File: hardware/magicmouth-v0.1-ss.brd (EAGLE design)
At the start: 100 x 80 mm, 28 parts, among them IC1 LM386N, IC2 ATMEGA168-20P, J1 1X2-3.5MM, Q1 16Mhz, U1 ARDUINOR3-NOIOREF-NOTEXT, X1 STEREOJACK

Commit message: added 5V jumper to v0.1 single sided board
added 5V jumper to v0.1 single sided board

added 5V jumper to v0.1 single sided board

added 5V jumper to v0.1 single sided board

added 5V jumper to v0.1 single sided board
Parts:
- moved C2 1.27 mm to (29.0, 55.9)
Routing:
- net N$5: track 21.8 -> 11.1 mm
- net +5V: track 78.5 -> 74.6 mm, vias 0 -> 2
- net GND: track 159.8 -> 160.3 mm
- net N$2: track 7.62 -> 8.15 mm
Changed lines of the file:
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@@
 <setting verticaltext="up"/>
 </settings>
-<grid distance="0.025" unitdist="inch" unit="inch" style="lines" multiple="1" display="yes" altdistance="0.025" altunitdist="inch" altunit="inch"/>
+<grid distance="0.025" unitdist="inch" unit="mm" style="lines" multiple="1" display="yes" altdistance="0.025" altunitdist="inch" altunit="inch"/>
 <layers>
 <layer number="1" name="Top" color="4" fill="1" visible="yes" active="yes"/>
@@
 <layer number="111" name="LPC17xx" color="7" fill="1" visible="yes" active="yes"/>
 <layer number="112" name="tSilk" color="7" fill="1" visible="yes" active="yes"/>
-<layer number="116" name="Patch_BOT" color="9" fill="4" visible="yes" active="yes"/>
+<layer number="116" name="centerDrill" color="9" fill="4" visible="yes" active="yes"/>
 <layer number="121" name="_tsilk" color="7" fill="1" visible="yes" active="yes"/>
 <layer number="122" name="_bsilk" color="7" fill="1" visible="yes" active="yes"/>
@@
 <wire x1="100" y1="80" x2="0" y2="80" width="0" layer="20"/>
 <wire x1="0" y1="80" x2="0" y2="0" width="0" layer="20"/>
-<text x="28.702" y="41.402" size="1.778" layer="51">Magic
-Mouth v0.1</text>
+<text x="76.962" y="22.352" size="1.4224" layer="51" rot="R90">Magic Mouth v0.1</text>
 <text x="42.164" y="14.097" size="0.8128" layer="21">RST</text>
 <text x="60.325" y="10.541" size="0.8128" layer="21">A0</text>
@@
 <text x="42.291" y="15.494" size="2.54" layer="21">_</text>
 <text x="50.8" y="21.59" size="1.27" layer="48">CC BY-SA 3.0</text>
-<text x="73.66" y="18.415" size="1.016" layer="51" rot="R180">http://tinyurl.com/magicmouth</text>
+<text x="73.025" y="32.385" size="1.016" layer="51" rot="R90">http://tinyurl.com/magicmouth</text>
 <text x="38.735" y="57.277" size="0.8128" layer="21" rot="R225">SCK</text>
 <text x="41.275" y="57.277" size="0.8128" layer="21" rot="R225">MISO</text>
 <text x="43.815" y="57.277" size="0.8128" layer="21" rot="R225">MOSI</text>
 <text x="46.355" y="57.277" size="0.8128" layer="21" rot="R225">RST</text>
+<hole x="24.13" y="12.7" drill="3.2"/>
+<hole x="25.4" y="60.96" drill="3.2"/>
+<hole x="76.2" y="45.72" drill="3.2"/>
+<hole x="76.2" y="17.78" drill="3.2"/>
 </plain>
 <attributes>
@@
 <attribute name="NAME" x="36.957" y="56.134" size="1.27" layer="25" ratio="10" rot="R90"/>
 </element>
-<element name="C2" library="resistor" package="E2,5-6" value="10uF" x="28.956" y="54.61" smashed="yes" rot="R90">
-<attribute name="NAME" x="25.527" y="53.467" size="1.27" layer="25" ratio="10" rot="R90"/>
+<element name="C2" library="resistor" package="E2,5-6" value="10uF" x="28.956" y="55.88" smashed="yes" rot="R90">
+<attribute name="NAME" x="25.527" y="54.737" size="1.27" layer="25" ratio="10" rot="R90"/>
 </element>
 <element name="C3" library="rcl" package="TT5D7L" value="220uF" x="24.13" y="37.465" smashed="yes" rot="R90">
@@
 <wire x1="30.48" y1="29.21" x2="29.21" y2="27.94" width="0.4064" layer="16"/>
 <contactref element="U1" pad="GND"/>
-<wire x1="23.114" y1="58.039" x2="33.655" y2="58.039" width="0.4064" layer="16"/>
 <wire x1="33.655" y1="58.039" x2="34.036" y2="58.42" width="0.4064" layer="16"/>
 <wire x1="34.036" y1="58.42" x2="34.163" y2="58.547" width="0.4064" layer="16"/>
@@
 <wire x1="36.703" y1="18.161" x2="39.37" y2="20.828" width="0.4064" layer="16"/>
 <contactref element="R3" pad="A"/>
-<wire x1="19.4" y1="55.88" x2="20.955" y2="55.88" width="0.4064" layer="16"/>
-<wire x1="23.114" y1="58.039" x2="20.955" y2="55.88" width="0.4064" layer="16"/>
 <wire x1="13.241" y1="26.57" x2="13.235" y2="26.57" width="0.4064" layer="16"/>
 <wire x1="13.235" y1="26.57" x2="10.795" y2="24.13" width="0.4064" layer="16"/>
@@
 <wire x1="35.56" y1="33.655" x2="39.37" y2="29.845" width="0.4064" layer="16"/>
 <wire x1="39.37" y1="29.845" x2="39.37" y2="20.828" width="0.4064" layer="16"/>
+<wire x1="19.4" y1="55.88" x2="31.496" y2="55.88" width="0.4064" layer="16"/>
+<wire x1="31.496" y1="55.88" x2="34.036" y2="58.42" width="0.4064" layer="16"/>
 </signal>
 <signal name="N$2">
@@
 <contactref element="R2" pad="2"/>
 <contactref element="C1" pad="1"/>
-<wire x1="28.956" y1="53.34" x2="34.036" y2="53.34" width="0.4064" layer="16"/>
 <wire x1="34.036" y1="53.34" x2="34.036" y2="55.88" width="0.4064" layer="16"/>
+<wire x1="34.036" y1="53.34" x2="30.226" y2="53.34" width="0.4064" layer="16"/>
+<wire x1="30.226" y1="53.34" x2="28.956" y2="54.61" width="0.4064" layer="16"/>
 </signal>
 <signal name="N$5">
 <contactref element="C2" pad="-"/>
 <contactref element="R3" pad="E"/>
-<wire x1="22.86" y1="55.88" x2="28.956" y2="55.88" width="0.4064" layer="16"/>
-<wire x1="22.86" y1="55.88" x2="20.955" y2="53.975" width="0.4064" layer="16"/>
-<wire x1="20.955" y1="53.975" x2="18.415" y2="53.975" width="0.4064" layer="16"/>
-<wire x1="18.415" y1="53.975" x2="17.78" y2="54.61" width="0.4064" layer="16"/>
-<wire x1="17.78" y1="54.61" x2="17.78" y2="56.515" width="0.4064" layer="16"/>
-<wire x1="17.78" y1="56.515" x2="18.415" y2="57.15" width="0.4064" layer="16"/>
-<wire x1="18.415" y1="57.15" x2="20.32" y2="57.15" width="0.4064" layer="16"/>
-<wire x1="20.32" y1="57.15" x2="20.955" y2="57.785" width="0.4064" layer="16"/>
-<wire x1="20.955" y1="57.785" x2="20.955" y2="59.69" width="0.4064" layer="16"/>
-<wire x1="19.4" y1="60.96" x2="19.685" y2="60.96" width="0.4064" layer="16"/>
-<wire x1="19.685" y1="60.96" x2="20.955" y2="59.69" width="0.4064" layer="16"/>
+<wire x1="28.956" y1="57.15" x2="24.13" y2="57.15" width="0.4064" layer="16"/>
+<wire x1="24.13" y1="57.15" x2="20.32" y2="60.96" width="0.4064" layer="16"/>
+<wire x1="20.32" y1="60.96" x2="19.4" y2="60.96" width="0.4064" layer="16"/>
 </signal>
 <signal name="N$4">
@@
 <contactref element="IC2" pad="20"/>
 <contactref element="R6" pad="2"/>
-<wire x1="54.61" y1="12.065" x2="53.975" y2="11.43" width="0.4064" layer="16"/>
-<wire x1="53.975" y1="11.43" x2="49.53" y2="11.43" width="0.4064" layer="16"/>
 <contactref element="R4" pad="2"/>
-<wire x1="49.53" y1="11.43" x2="48.26" y2="12.7" width="0.4064" layer="16"/>
-<wire x1="54.61" y1="12.065" x2="54.61" y2="28.829" width="0.4064" layer="16"/>
 <wire x1="54.61" y1="28.829" x2="60.706" y2="34.925" width="0.4064" layer="16"/>
 <wire x1="60.706" y1="34.925" x2="60.706" y2="36.68495" width="0.4064" layer="16"/>
-<wire x1="48.26" y1="12.7" x2="48.26" y2="13.97" width="0.4064" layer="16"/>
-<wire x1="48.26" y1="13.97" x2="44.45" y2="16.51" width="0.4064" layer="16"/>
 <wire x1="44.45" y1="16.51" x2="40.64" y2="16.51" width="0.4064" layer="16"/>
 <wire x1="43.815" y1="19.685" x2="40.64" y2="16.51" width="0.4064" layer="16"/>
@@
 <wire x1="48.26" y1="19.685" x2="48.26" y2="31.42315625" width="0.4064" layer="16"/>
 <wire x1="48.26" y1="31.42315625" x2="53.66684375" y2="36.83" width="0.4064" layer="16"/>
+<wire x1="48.26" y1="12.7" x2="48.26" y2="13.97" width="0.4064" layer="16"/>
+<wire x1="48.26" y1="13.97" x2="50.8" y2="16.51" width="0.4064" layer="16"/>
+<wire x1="50.8" y1="16.51" x2="54.61" y2="16.51" width="0.4064" layer="1"/>
+<wire x1="54.61" y1="16.51" x2="54.61" y2="28.829" width="0.4064" layer="16"/>
+<via x="50.8" y="16.51" extent="1-16" drill="0.6" diameter="1.27"/>
+<via x="54.61" y="16.51" extent="1-16" drill="0.6" diameter="1.27"/>
+<wire x1="44.45" y1="16.51" x2="45.72" y2="16.51" width="0.4064" layer="16"/>
+<wire x1="45.72" y1="16.51" x2="48.26" y2="13.97" width="0.4064" layer="16"/>
 </signal>
 <signal name="GND1">
@@
 </board>
 </drawing>
-<compatibility>
-<note version="6.3" minversion="6.2.2" severity="warning">
-Since Version 6.2.2 text objects can contain more than one line,
-which will not be processed correctly with this version.
-</note>
-</compatibility>
 </eagle>

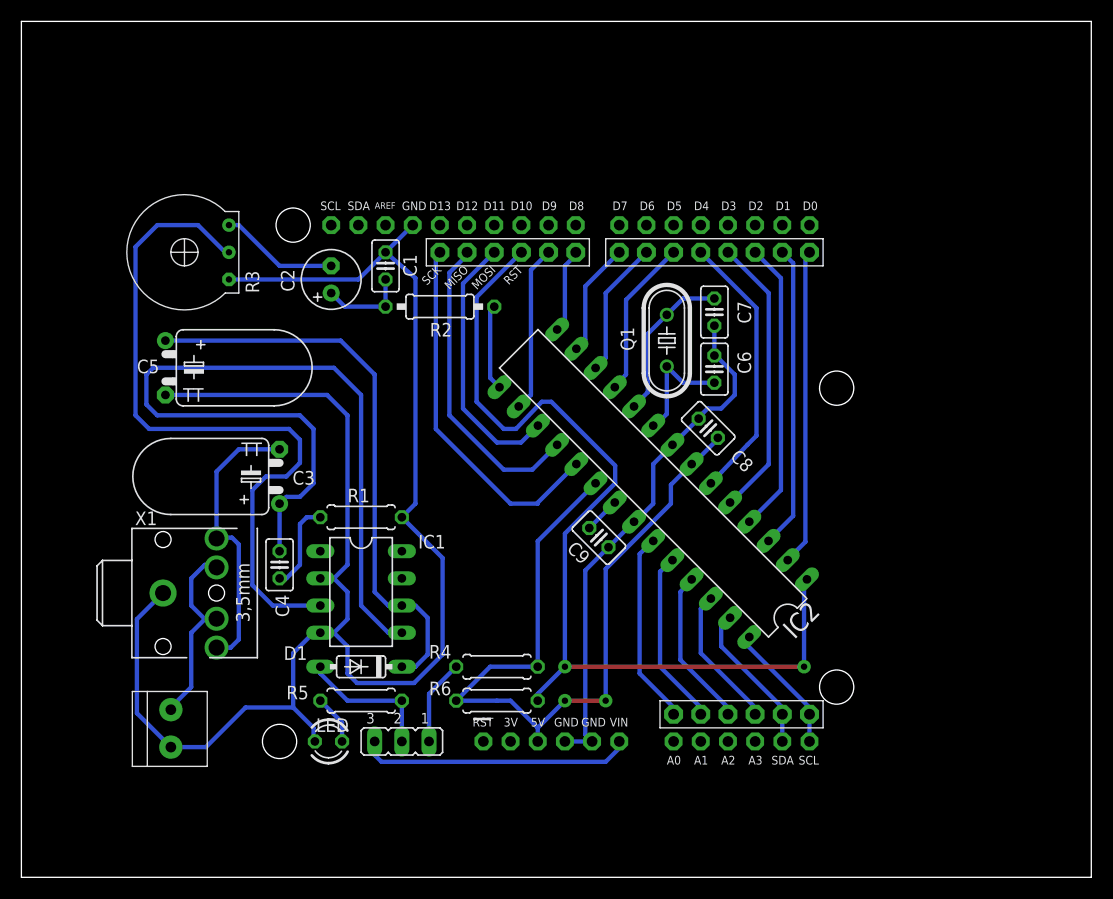
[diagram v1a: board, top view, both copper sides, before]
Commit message: added programming jumpers
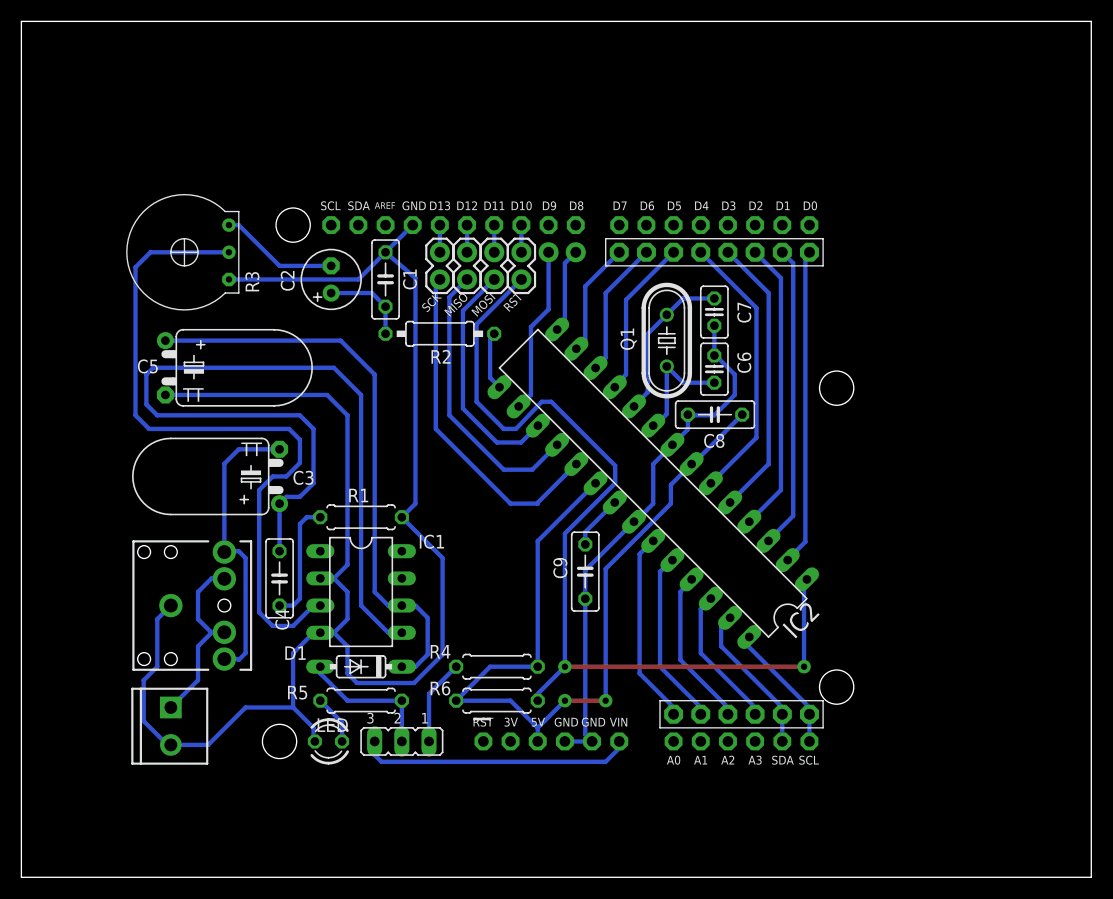
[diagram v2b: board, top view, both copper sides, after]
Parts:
- removed X1: STEREOJACK, adafruit:STX3100
- added JP5, JP6, JP7, JP8: (no value), SparkFun-Passives:1X02
- added U$2: AUDIO-JACK2PTH, SparkFun-Connectors:AUDIO-JACK
- C1: device resistor:C025-025X050 -> resistor:C050-025X075
- C4, C8, C9: device rcl:C025-025X050 -> resistor:C050-025X075
- J1: value 1X2-3.5MM -> (none); device adafruit:1X2-3.5MM -> SparkFun-Connectors:SCREWTERMINAL-3.5MM-2
- JP3: device adafruit:1X06-BIG -> SparkFun-Connectors:1X02_NO_SILK
- moved JP3 6.35 mm to (51.8, 58.4)
- moved C9 3.42 mm to (52.7, 28.6), turned to 270 degrees
- moved R2 2.54 mm to (39.1, 50.8)
- moved J1 1.90 mm to (14.0, 15.9)
- moved C8 1.42 mm to (64.8, 43.2), turned to 180 degrees
- moved C4 1.27 mm to (24.1, 27.9)
- moved C1 1.27 mm to (34.0, 55.9)
- moved U$1 0.63 mm to (57.8, 25.4)
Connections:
- new net N$25: JP5.1, U1.D13
- new net N$26: JP6.1, U1.D12
- new net N$28: JP7.1, U1.D11
- new net N$29: JP8.1, U1.D10
- net GND: now also J1.2, U$2.SLEEVE; no longer J1.1, X1.1
- net MISO: now also JP6.2; no longer JP3.5
- net MOSI: now also JP7.2; no longer JP3.4
- net N$3: now also J1.1, U$2.RSH, U$2.TSH; no longer J1.2, X1.3, X1.4
- net N$8: now also U$2.RING, U$2.TIP; no longer X1.2, X1.5
- net SCK: now also JP5.2; no longer JP3.6
- net SS: now also JP8.2; no longer JP3.3
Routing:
- net +5V: track 74.6 -> 77.7 mm
- net N$4: track 8.41 -> 11.3 mm
- net SIGNAL: track 8.05 -> 5.51 mm
- net MISO: track 29.1 -> 26.5 mm
- net SCK: track 34.3 -> 31.7 mm
- net N$29: track 0.00 -> 2.54 mm
- net N$28: track 0.00 -> 2.54 mm
- net N$26: track 0.00 -> 2.54 mm
- net N$25: track 0.00 -> 2.54 mm
- net MOSI: track 24.8 -> 22.2 mm
- net SS: track 88.9 -> 86.3 mm
- net N$14: track 3.37 -> 5.06 mm
- net GND: track 160.3 -> 158.8 mm
- net N$9: track 66.4 -> 65.3 mm
- net GND1: track 49.1 -> 49.9 mm
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
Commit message: reset switch on ss board; optional capacitor
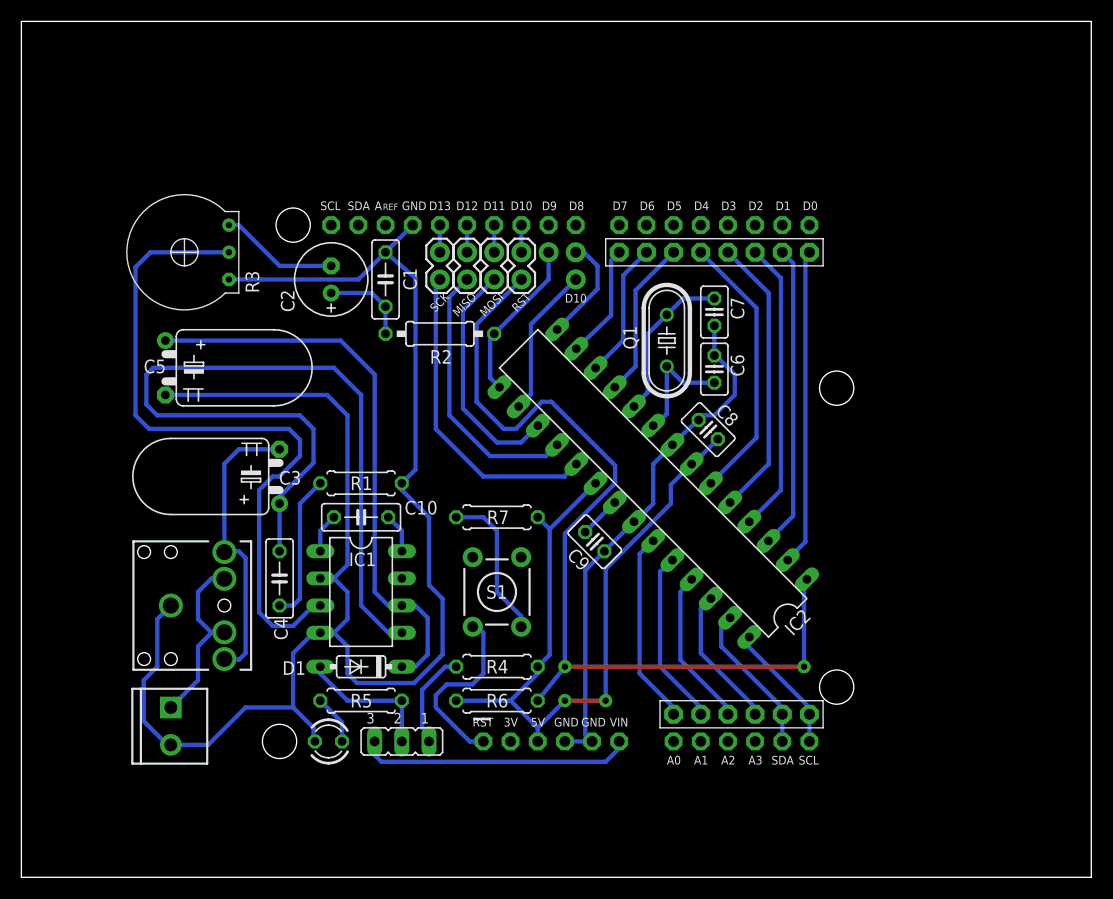
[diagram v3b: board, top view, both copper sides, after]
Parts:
- added C10: 1uF, resistor:C050-025X075
- added JP9: M01SMDNS, SparkFun-Connectors:1X01NS
- added R7: 4K7, rcl:0207/7
- added S1: SWITCH-MOMENTARY-2PTH, SparkFun-Electromechanical:TACTILE-PTH
- C2: device resistor:E2,5-6 -> rcl:E2,5-7
- C8, C9: device resistor:C050-025X075 -> rcl:C025-025X050
- moved R1 3.17 mm to (31.8, 36.8)
- moved C9 2.93 mm to (53.6, 31.4), turned to 315 degrees
- moved C8 1.53 mm to (64.2, 41.8), turned to 135 degrees
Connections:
- new net N$34: R7.2, S1.3
- new net N$35: S1.1, U1.RESET
- new net N$36: C10.2, IC1.8
- new net N$37: C10.1, IC1.1
- net +5V: now also R7.1
- net N$12: now also JP9.1; no longer JP3.2
- net SIGNAL: now also JP3.2
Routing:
- net N$35: track 0.00 -> 17.2 mm
- net N$34: track 0.00 -> 14.2 mm
- net SIGNAL: track 5.51 -> 15.2 mm
- net +5V: track 77.7 -> 71.4 mm
- net N$36: track 0.00 -> 3.70 mm
- net N$37: track 0.00 -> 3.70 mm
- net N$4: track 11.3 -> 13.8 mm
- net N$24: track 7.94 -> 10.1 mm
- net SCK: track 31.7 -> 29.6 mm
- net N$12: track 15.6 -> 14.1 mm
- net N$14: track 5.06 -> 3.91 mm
- net N$7: track 8.04 -> 9.16 mm
- net MISO: track 26.5 -> 25.5 mm
- net GND1: track 49.9 -> 49.0 mm
- net N$1: track 78.8 -> 78.0 mm
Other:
- board text added: "A"
- board text added: "REF"
- board text removed: "AREF"

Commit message: 220K resistor in series with gain control
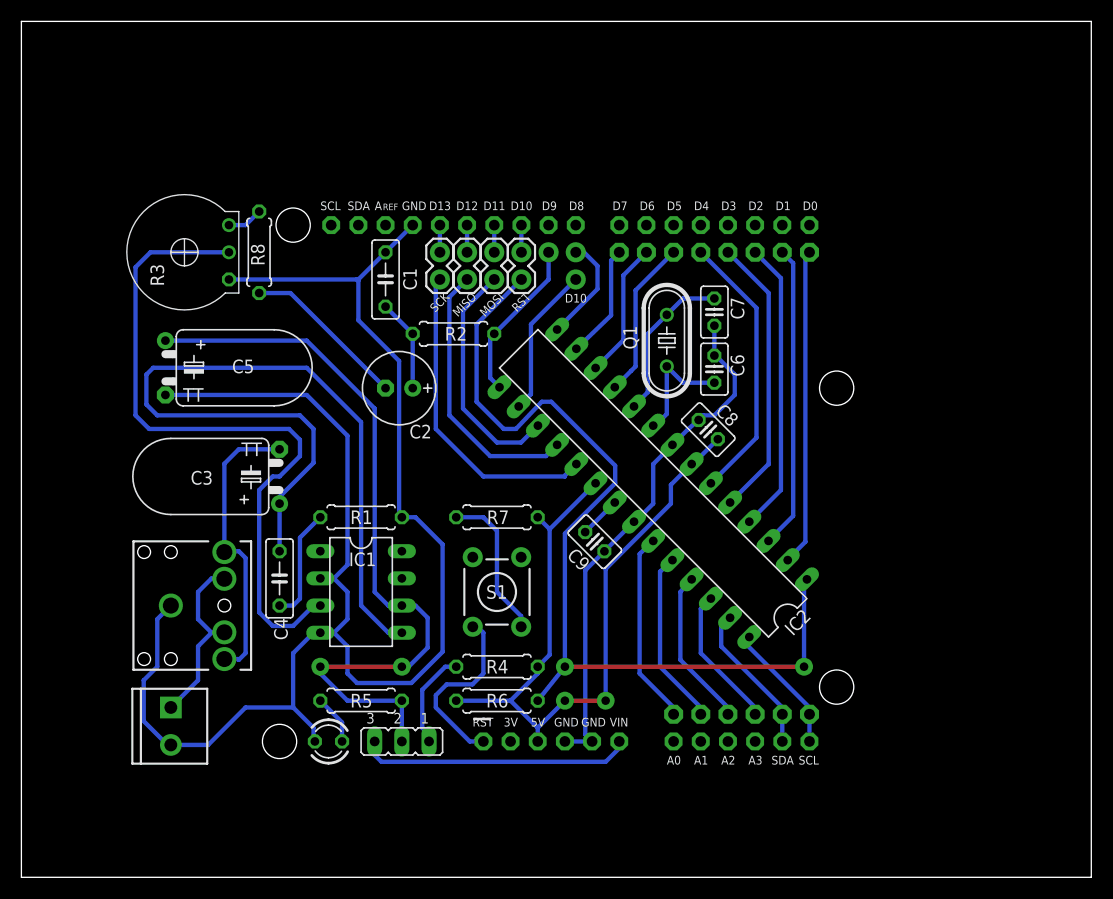
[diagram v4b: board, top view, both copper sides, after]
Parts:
- removed C10: 1uF, resistor:C050-025X075
- removed D1: 1N4148, diode:DO35-7
- added R8: 220K, rcl:0207/7
- JP2: device adafruit:1X08-BIG -> adafruit:1X08-CLEANBIG
- JP4: device adafruit:1X06-BIG -> adafruit:1X06-CLEANBIG
- R2: device resistor:0207/10 -> rcl:0207/7
- moved C2 12.0 mm to (35.3, 45.7), turned to 180 degrees
- moved R1 3.17 mm to (31.8, 33.7)
- moved R2 1.27 mm to (40.4, 50.8)
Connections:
- removed net N$27: D1.A, JP1.2, R5.2
- removed net N$37: C10.1, IC1.1
- net N$36: now also R3.E, R8.2; no longer C10.2, IC1.8
- net N$5: now also R8.1; no longer R3.E
- net VS: now also JP1.2, R5.2; no longer D1.C
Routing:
- net VS: track 53.5 -> 72.0 mm, vias 0 -> 2
- net N$27: track 13.1 -> 0.00 mm
- net N$5: track 11.1 -> 15.5 mm
- net N$37: track 3.70 -> 0.00 mm
- net N$4: track 13.8 -> 10.6 mm
- net GND: track 158.8 -> 155.7 mm
- net N$1: track 78.0 -> 76.5 mm
- net N$2: track 8.15 -> 8.67 mm
